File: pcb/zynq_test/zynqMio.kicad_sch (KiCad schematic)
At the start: 20 parts, among them SW201 SW_SPDT, SW202 SW_SPDT, SW203 SW_SPDT, U1 XC7Z020-2CLG400I

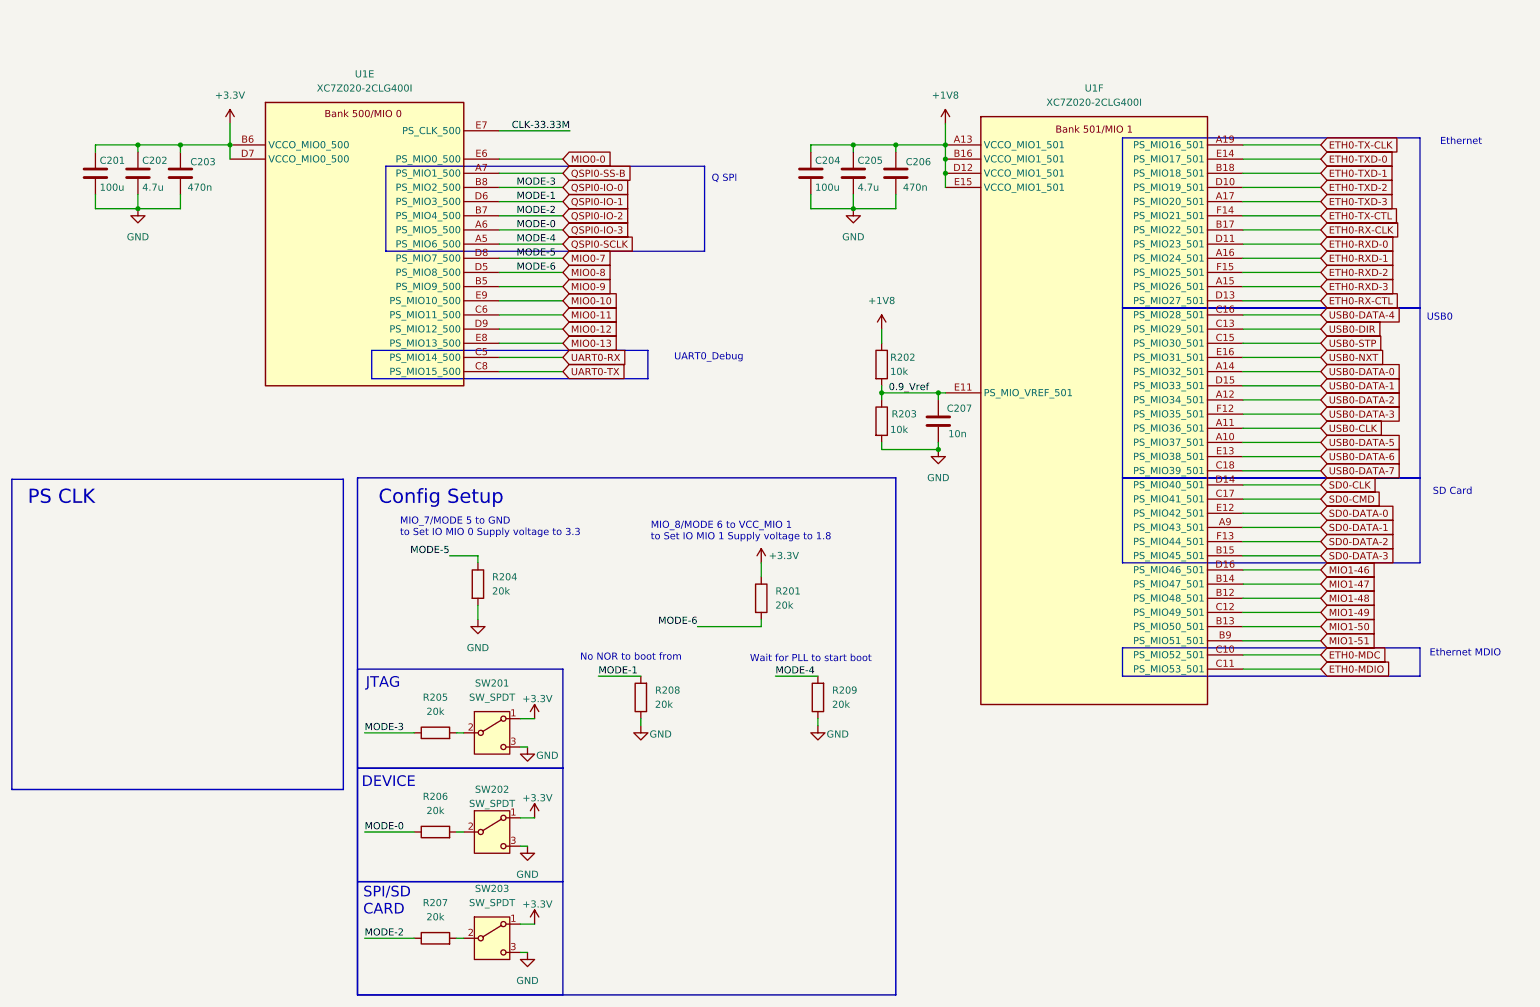
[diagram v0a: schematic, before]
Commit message: Changed MIO signals to Buses
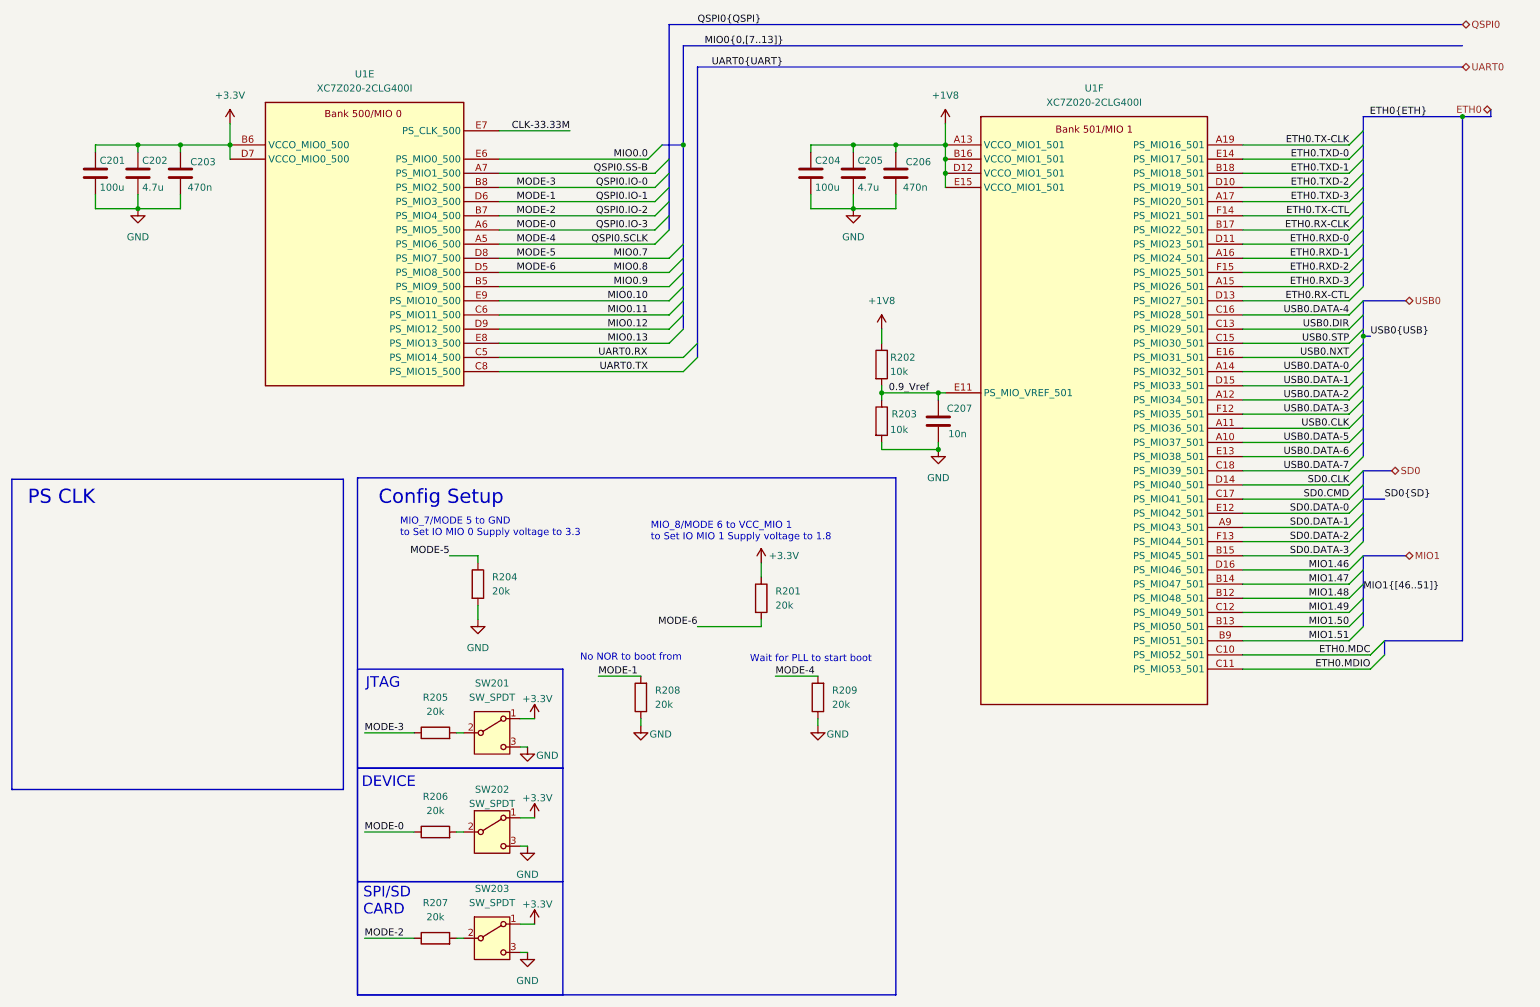
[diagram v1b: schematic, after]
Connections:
- net ETH0-MDC renamed ETH0.MDC
- net ETH0-MDIO renamed ETH0.MDIO
- net ETH0-RX-CLK renamed ETH0.RX-CLK
- net ETH0-RX-CTL renamed ETH0.RX-CTL
- net ETH0-RXD-0 renamed ETH0.RXD-0
- net ETH0-RXD-1 renamed ETH0.RXD-1
- net ETH0-RXD-2 renamed ETH0.RXD-2
- net ETH0-RXD-3 renamed ETH0.RXD-3
- net ETH0-TX-CLK renamed ETH0.TX-CLK
- net ETH0-TX-CTL renamed ETH0.TX-CTL
- net ETH0-TXD-0 renamed ETH0.TXD-0
- net ETH0-TXD-1 renamed ETH0.TXD-1
- net ETH0-TXD-2 renamed ETH0.TXD-2
- net ETH0-TXD-3 renamed ETH0.TXD-3
- net MIO0-0 renamed MIO0.0
- net MIO0-10 renamed MIO0.10
- net MIO0-11 renamed MIO0.11
- net MIO0-12 renamed MIO0.12
- net MIO0-13 renamed MIO0.13
- net MIO0-7 renamed MIO0.7
- net MIO0-8 renamed MIO0.8
- net MIO0-9 renamed MIO0.9
- net MIO1-46 renamed MIO1.46
- net MIO1-47 renamed MIO1.47
- net MIO1-48 renamed MIO1.48
- net MIO1-49 renamed MIO1.49
- net MIO1-50 renamed MIO1.50
- net MIO1-51 renamed MIO1.51
- net QSPI0-IO-0 renamed MODE-3
- net QSPI0-IO-1 renamed MODE-1
- net QSPI0-IO-2 renamed MODE-2
- net QSPI0-IO-3 renamed MODE-0
- net QSPI0-SCLK renamed MODE-4
- net QSPI0-SS-B renamed QSPI0.SS-B
- net SD0-CLK renamed SD0.CLK
- net SD0-CMD renamed SD0.CMD
- net SD0-DATA-0 renamed SD0.DATA-0
- net SD0-DATA-1 renamed SD0.DATA-1
- net SD0-DATA-2 renamed SD0.DATA-2
- net SD0-DATA-3 renamed SD0.DATA-3
- net UART0-RX renamed UART0.RX
- net UART0-TX renamed UART0.TX
- net USB0-CLK renamed USB0.CLK
- net USB0-DATA-0 renamed USB0.DATA-0
- net USB0-DATA-1 renamed USB0.DATA-1
- net USB0-DATA-2 renamed USB0.DATA-2
- net USB0-DATA-3 renamed USB0.DATA-3
- net USB0-DATA-4 renamed USB0.DATA-4
- net USB0-DATA-5 renamed USB0.DATA-5
- net USB0-DATA-6 renamed USB0.DATA-6
- net USB0-DATA-7 renamed USB0.DATA-7
- net USB0-DIR renamed USB0.DIR
- net USB0-NXT renamed USB0.NXT
- net USB0-STP renamed USB0.STP
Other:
- note removed: "Ethernet"
- note removed: "Ethernet MDIO"
- note removed: "Q SPI"
- note removed: "SD Card"
- note removed: "UART0_Debug"
- note removed: "USB0"

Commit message: Finished PS, started on PWR
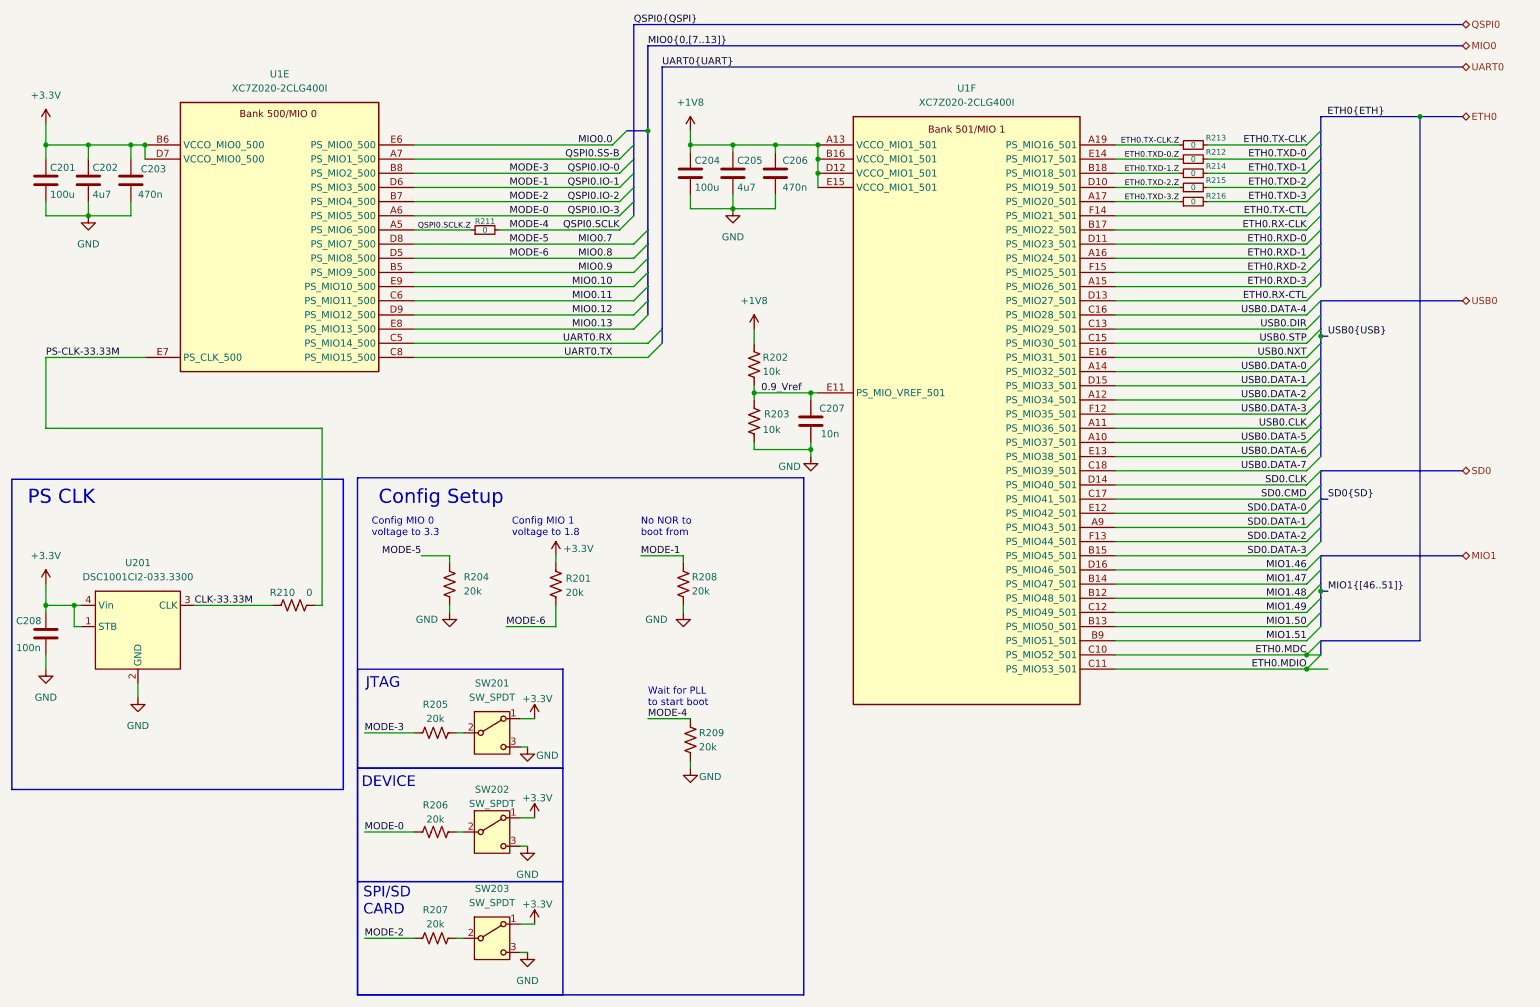
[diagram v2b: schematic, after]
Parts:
- added C208: 100n, symbol Device:C
- added R210: 0, symbol Device:R_US
- added R211, R212, R213, R214, R215, R216: 0, symbol Device:R_Small
- added U201: DSC1001CI2-033.3300, symbol other:DSC1001CI2-033.3300
- C202, C205: value 4.7u -> 4u7
- R201, R202, R203, R204, R205, R206, R207, R208, R209: symbol Device:R -> Device:R_US
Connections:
- net +3.3V: now also C208.1, U201.1 (STB), U201.4 (Vin)
- net CLK-33.33M: now also R210.1, U201.3 (CLK); no longer U1.E7 (PS_CLK_500)
- net ETH0.TX-CLK: now also R213.2; no longer U1.A19 (PS_MIO16_501)
- net ETH0.TXD-0: now also R212.2; no longer U1.E14 (PS_MIO17_501)
- net ETH0.TXD-1: now also R214.2; no longer U1.B18 (PS_MIO18_501)
- net ETH0.TXD-2: now also R215.2; no longer U1.D10 (PS_MIO19_501)
- net ETH0.TXD-3: now also R216.2; no longer U1.A17 (PS_MIO20_501)
- net GND: now also C208.2, U201.2 (GND)
- net MODE-4: now also R211.2; no longer U1.A5 (PS_MIO6_500)
- new net ETH0.TX-CLK.Z: R213.1, U1.A19 (PS_MIO16_501)
- new net ETH0.TXD-0.Z: R212.1, U1.E14 (PS_MIO17_501)
- new net ETH0.TXD-1.Z: R214.1, U1.B18 (PS_MIO18_501)
- new net ETH0.TXD-2.Z: R215.1, U1.D10 (PS_MIO19_501)
- new net ETH0.TXD-3.Z: R216.1, U1.A17 (PS_MIO20_501)
- new net PS-CLK-33.33M: R210.2, U1.E7 (PS_CLK_500)
- new net QSPI0.SCLK.Z: R211.1, U1.A5 (PS_MIO6_500)
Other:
- note added: "Config MIO 0 voltage to 3.3"
- note added: "Config MIO 1 voltage to 1.8"
- note removed: "MIO_7/MODE 5 to GND to Set IO MIO 0 Supply voltage to 3.3"
- note removed: "MIO_8/MODE 6 to VCC_MIO 1 to Set IO MIO 1 Supply voltage to 1.8"
- moved on the sheet: C201, C202, C203, C204, C205, C206, C207, U1E, U1F

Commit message: Finished FPGA decouploing, and jtag programmer
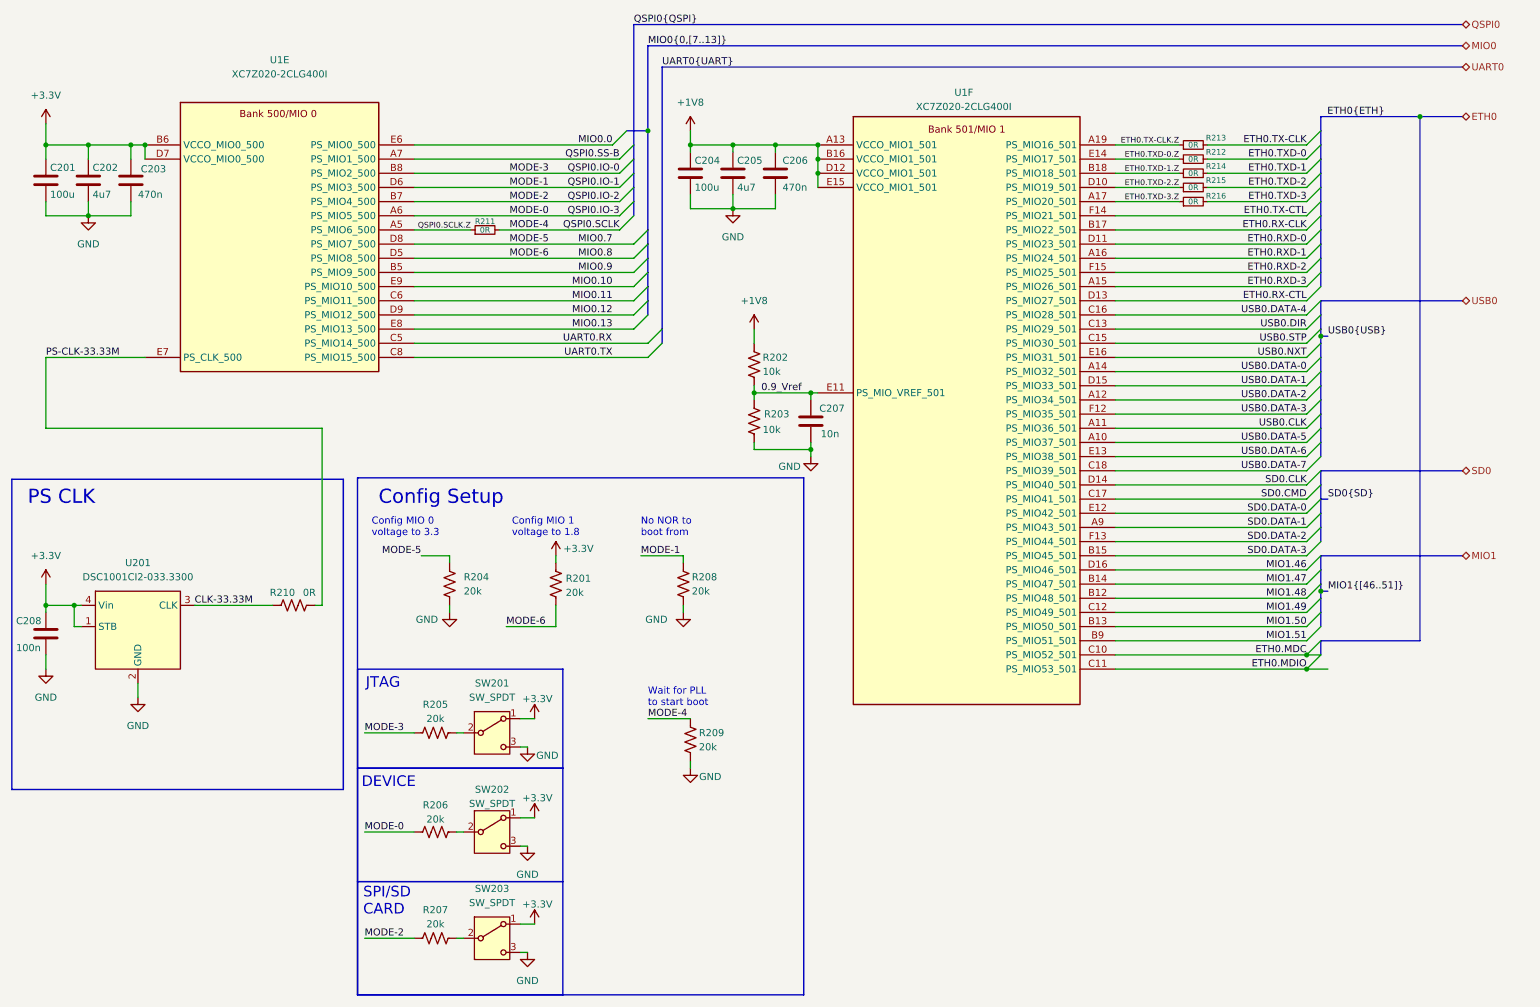
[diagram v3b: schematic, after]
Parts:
- R210, R211, R212, R213, R214, R215, R216: value 0 -> 0R
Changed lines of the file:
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@@
 			)
 		)
-		(property "Value" "0"
+		(property "Value" "0R"
 			(at 68.834 120.904 90)
 			(effects
@@
 			)
 		)
-		(property "Value" "0"
+		(property "Value" "0R"
 			(at 227.33 45.72 90)
 			(effects
@@
 	)
 	(symbol
+		(lib_name "XC7Z020-2CLG400I_1")
 		(lib_id "zynq:XC7Z020-2CLG400I")
 		(at 63.5 59.69 0)
@@
 		(fields_autoplaced yes)
 		(property "Reference" "U1"
-			(at 63.5 27.94 0)
+			(at 63.5 25.4 0)
 			(effects
 				(font
@@
 		)
 		(property "Value" "XC7Z020-2CLG400I"
-			(at 63.5 30.48 0)
+			(at 63.5 27.94 0)
 			(effects
 				(font
@@
 		(instances
 			(project ""
+				(path "/0637578d-4ce5-4d31-b973-2de977269ea5/571469d6-3394-40d8-b17a-7dc7211f29f5"
+					(reference "U1")
+					(unit 5)
+				)
 				(path "/0637578d-4ce5-4d31-b973-2de977269ea5/db3711b0-f4a6-4694-bd1d-6c88710ed953"
 					(reference "U1")
@@
 			)
 		)
-		(property "Value" "0"
+		(property "Value" "0R"
 			(at 227.33 50.8 90)
 			(effects
@@
 			)
 		)
-		(property "Value" "0"
+		(property "Value" "0R"
 			(at 227.33 43.18 90)
 			(effects
@@
 		(on_board yes)
 		(dnp no)
-		(fields_autoplaced yes)
 		(property "Reference" "U1"
-			(at 186.69 30.48 0)
+			(at 186.182 31.242 0)
 			(effects
 				(font
@@
 		)
 		(property "Value" "XC7Z020-2CLG400I"
-			(at 186.69 33.02 0)
+			(at 186.182 33.782 0)
 			(effects
 				(font
@@
 		(instances
 			(project ""
+				(path "/0637578d-4ce5-4d31-b973-2de977269ea5/571469d6-3394-40d8-b17a-7dc7211f29f5"
+					(reference "U1")
+					(unit 6)
+				)
 				(path "/0637578d-4ce5-4d31-b973-2de977269ea5/db3711b0-f4a6-4694-bd1d-6c88710ed953"
 					(reference "U1")
@@
 			)
 		)
-		(property "Value" "0"
+		(property "Value" "0R"
 			(at 227.33 48.26 90)
 			(effects
@@
 			)
 		)
-		(property "Value" "0"
+		(property "Value" "0R"
 			(at 227.33 40.64 90)
 			(effects
@@
 			)
 		)
-		(property "Value" "0"
+		(property "Value" "0R"
 			(at 100.33 55.88 90)
 			(effects

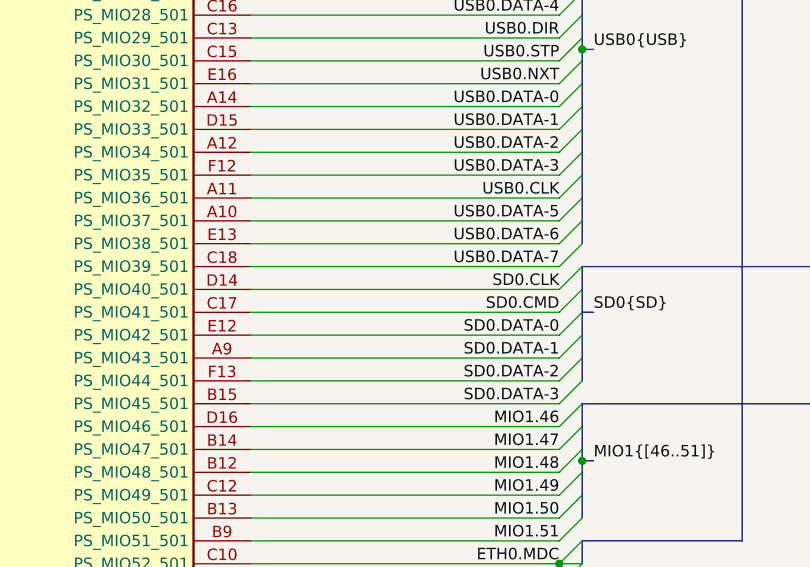
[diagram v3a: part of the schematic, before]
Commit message: Finished boot media, added structure for IO
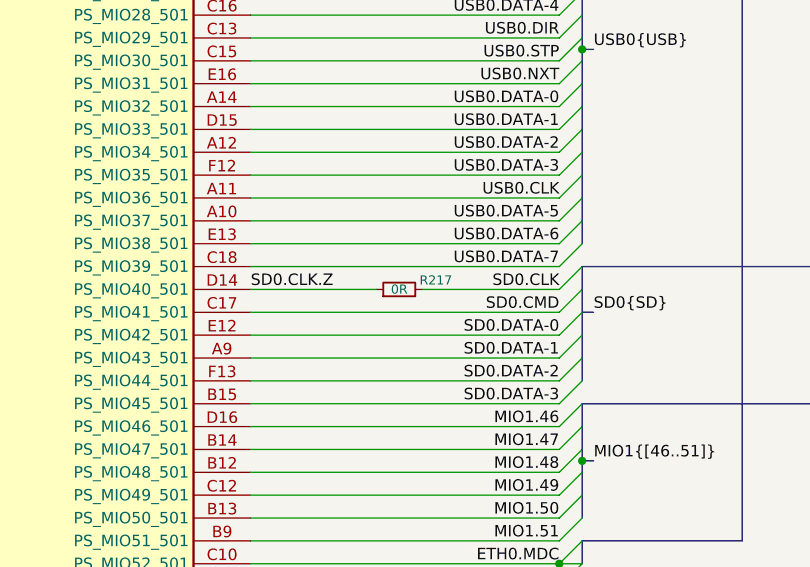
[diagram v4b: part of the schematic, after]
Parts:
- added R217: 0R, symbol Device:R_Small
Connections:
- net SD0.CLK: now also R217.2; no longer U1.D14 (PS_MIO40_501)
- new net SD0.CLK.Z: R217.1, U1.D14 (PS_MIO40_501)
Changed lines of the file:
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@@
 		)
 	)
+	(wire
+		(pts
+			(xy 232.41 101.6) (xy 247.65 101.6)
+		)
+		(stroke
+			(width 0)
+			(type default)
+		)
+	)
 	(bus
 		(pts
@@
 	(wire
 		(pts
-			(xy 213.36 101.6) (xy 247.65 101.6)
+			(xy 213.36 101.6) (xy 227.33 101.6)
 		)
 		(stroke
@@
 		)
 	)
+	(label "SD0.CLK.Z"
+		(at 213.36 101.6 0)
+		(effects
+			(font
+				(size 1.27 1.27)
+			)
+			(justify left bottom)
+		)
+	)
 	(label "MIO0.12"
 		(at 123.19 71.12 180)
@@
 					(unit 1)
 				)
+			)
+		)
+	)
+	(symbol
+		(lib_id "Device:R_Small")
+		(at 229.87 101.6 90)
+		(unit 1)
+		(exclude_from_sim no)
+		(in_bom yes)
+		(on_board yes)
+		(dnp no)
+		(property "Reference" "R217"
+			(at 233.934 100.584 90)
+			(effects
+				(font
+					(size 1.016 1.016)
+				)
+			)
+		)
+		(property "Value" "0R"
+			(at 229.87 101.6 90)
+			(effects
+				(font
+					(size 1.016 1.016)
+				)
+			)
+		)
+		(property "Footprint" ""
+			(at 229.87 101.6 0)
+			(effects
+				(font
+					(size 1.27 1.27)
+				)
+				(hide yes)
+			)
+		)
+		(property "Datasheet" "~"
+			(at 229.87 101.6 0)
+			(effects
+				(font
+					(size 1.27 1.27)
+				)
+				(hide yes)
+			)
+		)
+		(property "Description" "Resistor, small symbol"
+			(at 229.87 101.6 0)
+			(effects
+				(font
+					(size 1.27 1.27)
+				)
+				(hide yes)
+			)
+		)
+		(pin "1"
+		)
+		(pin "2"
+		)
+		(instances
+			(project "zynq_test"
+				(path "/0637578d-4ce5-4d31-b973-2de977269ea5/db3711b0-f4a6-4694-bd1d-6c88710ed953"
+					(reference "R217")
+					(unit 1)
+				)
